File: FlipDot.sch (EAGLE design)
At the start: 96 parts, among them X1 FAC64S

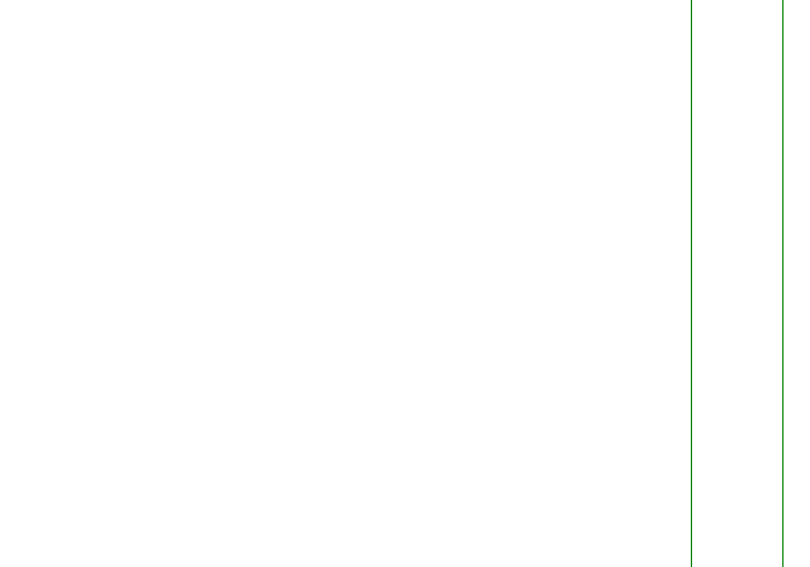
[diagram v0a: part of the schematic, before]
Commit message: Initial HW Rev2 commit.
This Rev is a work in progress and is not ready to be sent to fab.
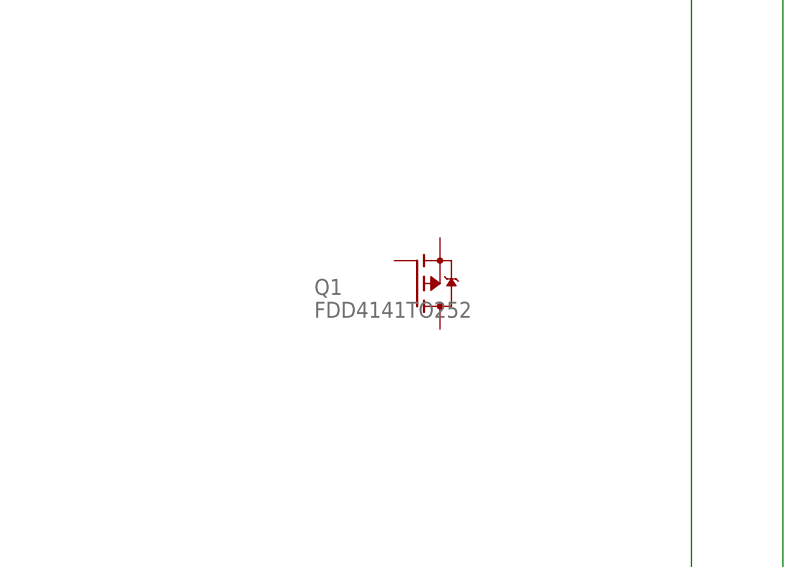
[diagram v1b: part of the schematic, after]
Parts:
- added Q1: FDD4141TO252, transistor-fet:FDD4141TO252
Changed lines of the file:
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@@
 <part name="C13" library="rcl" deviceset="C-US" device="C2012"/>
 <part name="GND16" library="supply1" deviceset="GND" device=""/>
+<part name="Q1" library="transistor-fet" deviceset="FDD4141" device="TO252"/>
 </parts>
 <sheets>
@@
 <instance part="C13" gate="G$1" x="1122.68" y="353.06" rot="R90"/>
 <instance part="GND16" gate="1" x="1140.46" y="345.44" rot="R180"/>
+<instance part="Q1" gate="G$1" x="-78.74" y="276.86"/>
 </instances>
 <busses>
